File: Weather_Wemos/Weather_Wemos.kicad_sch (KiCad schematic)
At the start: 20 parts, among them J1 Pwr In, J2 12V, J3 Rain 3 Adv, J4 WIND, J5 RAIN 1, J6 Rain 2 Serial, U1 WeMos_D1_mini, U2 L7805

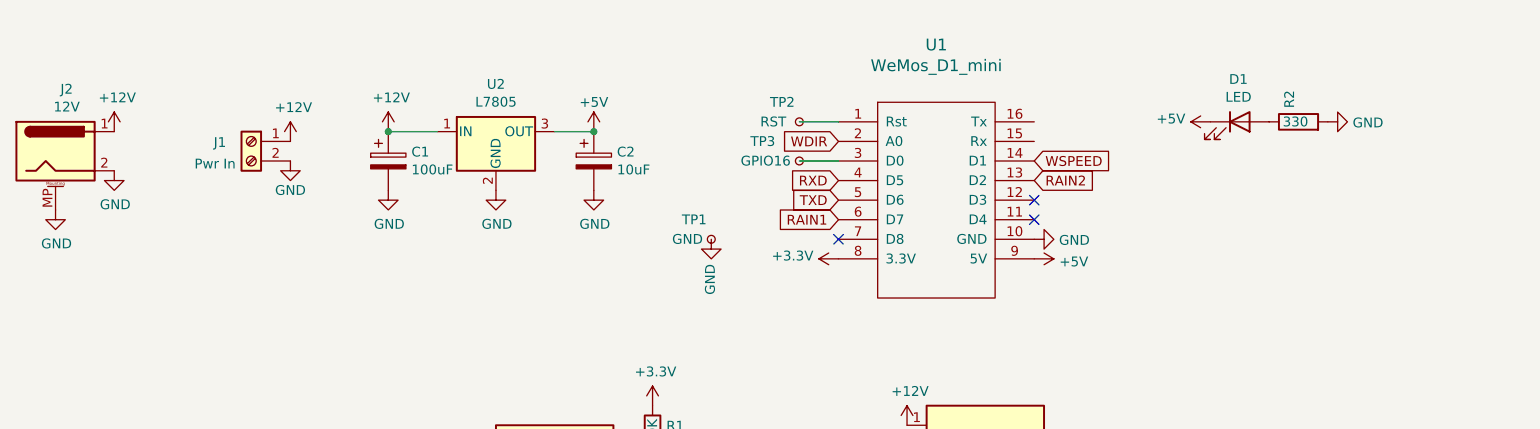
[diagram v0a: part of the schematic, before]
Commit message: added temperature sensor
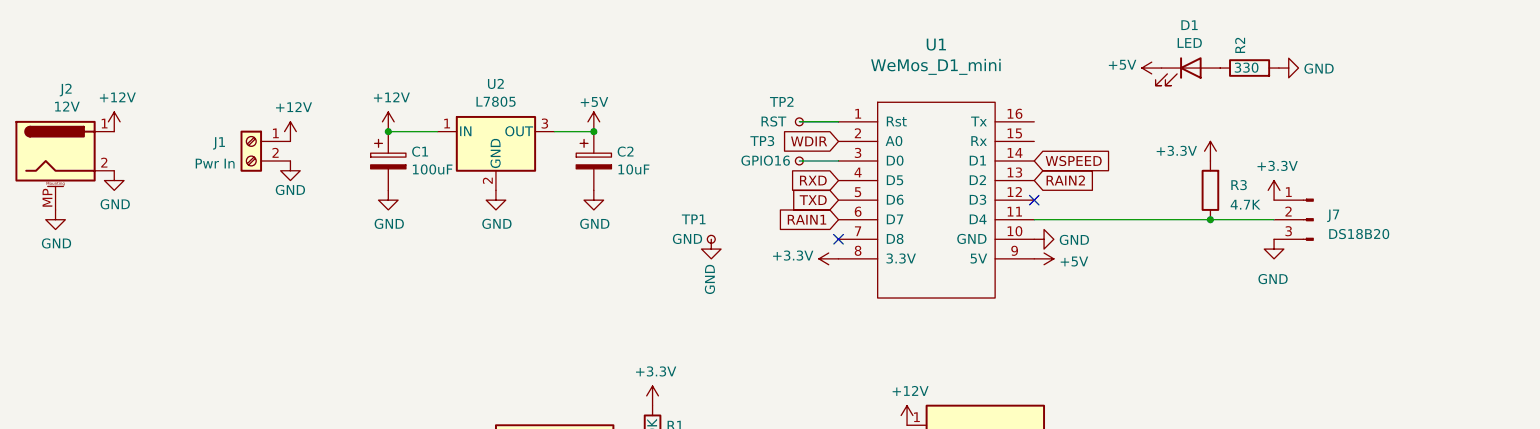
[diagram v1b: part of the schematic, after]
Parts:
- added J7: DS18B20, Connector_JST:JST_XH_B3B-XH-A_1x03_P2.50mm_Vertical, symbol Connector:Conn_01x03_Pin
- added R3: 4.7K, Resistor_THT:R_Axial_DIN0207_L6.3mm_D2.5mm_P7.62mm_Horizontal, symbol Device:R
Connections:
- net +3V3: now also J7.1 (Pin_1), R3.2
- net GND: now also J7.3 (Pin_3)
- net at U1.11 (D4): now also J7.2 (Pin_2), R3.1
- no-connect marks 3 -> 2
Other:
- moved on the sheet: D1, R2

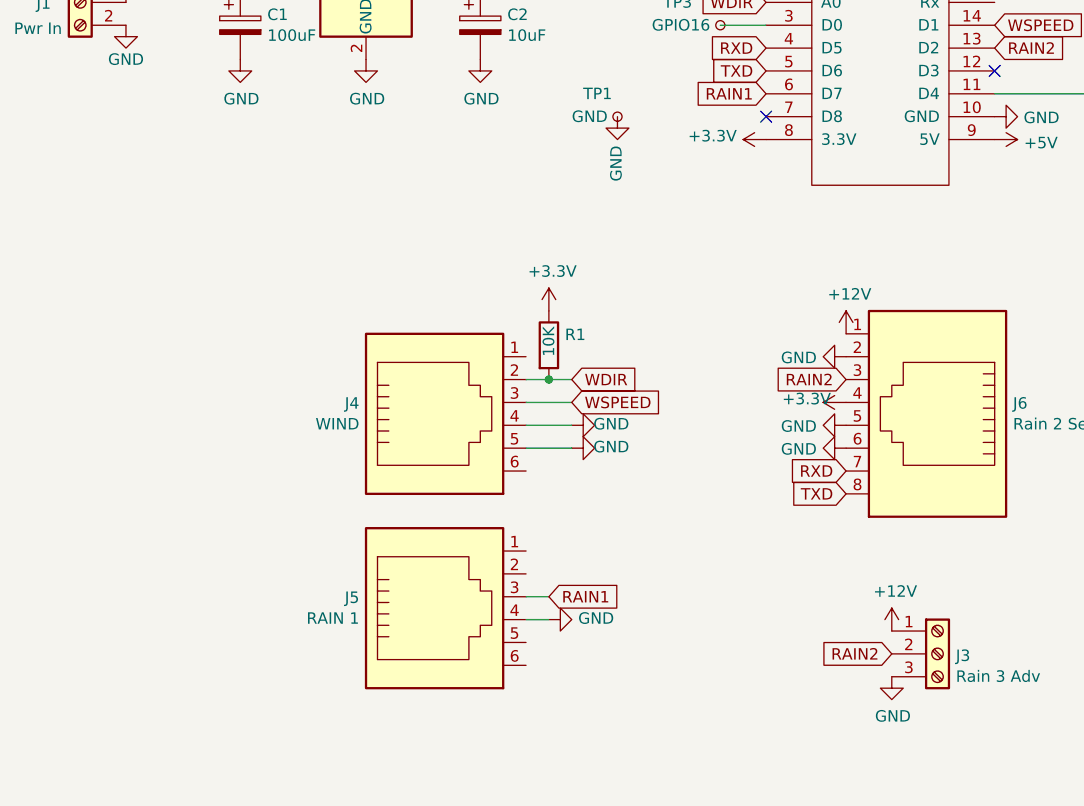
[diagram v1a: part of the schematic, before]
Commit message: add plug in 3 to 4 adapter
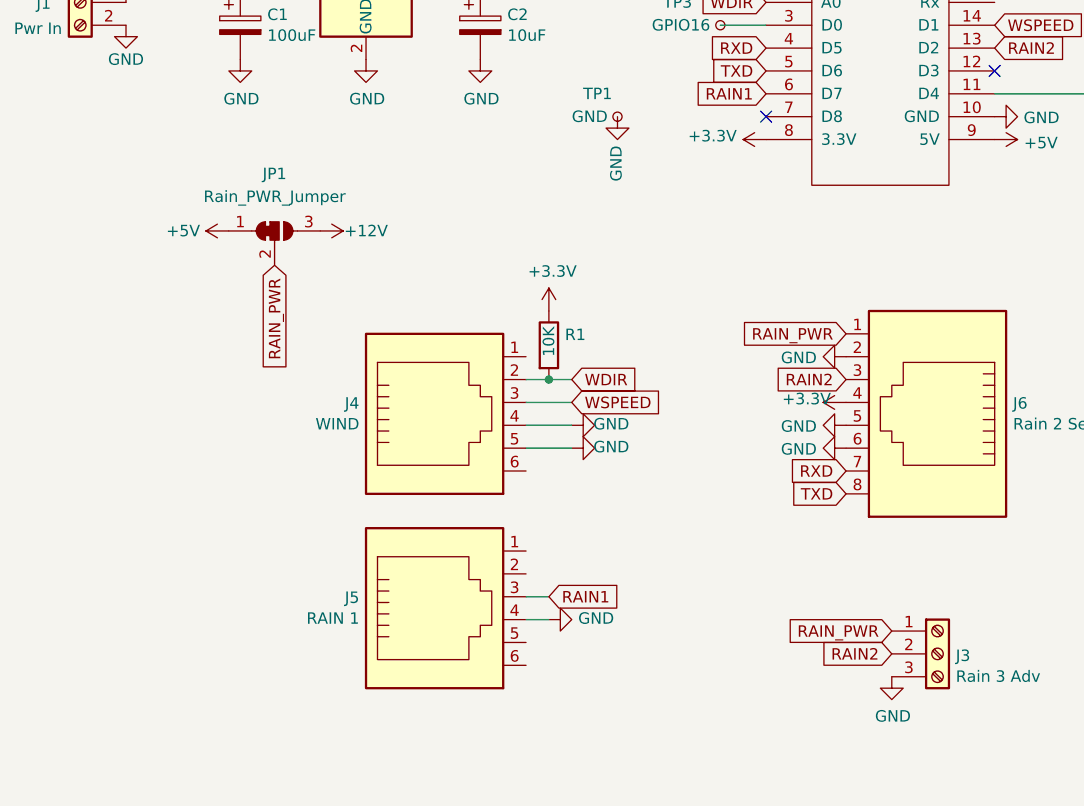
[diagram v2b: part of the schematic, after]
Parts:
- added JP1: Rain_PWR_Jumper, Jumper:SolderJumper-3_P1.3mm_Bridged2Bar12_RoundedPad1.0x1.5mm_NumberLabels, symbol Jumper:SolderJumper_3_Bridged12
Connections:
- net +12V: now also JP1.3 (B); no longer J3.1 (Pin_1), J6.1
- net +5V: now also JP1.1 (A)
- new net RAIN_PWR: J3.1 (Pin_1), J6.1, JP1.2 (C)
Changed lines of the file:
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@@
     (stroke (width 0) (type default))
+  )
+  (global_label "RAIN_PWR" (shape input) (at 144.78 86.36 180) (fields_autoplaced)
+    (effects (font (size 1.27 1.27)) (justify right))
+    (property "Intersheetrefs" "${INTERSHEET_REFS}" (at 133.2755 86.36 0)
+      (effects (font (size 1.27 1.27)) (justify right) hide)
+    )
   )
   (global_label "TXD" (shape input) (at 144.78 104.14 180) (fields_autoplaced)
@@
     )
   )
+  (global_label "RAIN_PWR" (shape input) (at 149.86 119.38 180) (fields_autoplaced)
+    (effects (font (size 1.27 1.27)) (justify right))
+    (property "Intersheetrefs" "${INTERSHEET_REFS}" (at 138.3555 119.38 0)
+      (effects (font (size 1.27 1.27)) (justify right) hide)
+    )
+  )
   (global_label "RAIN2" (shape input) (at 161.29 54.61 0) (fields_autoplaced)
     (effects (font (size 1.27 1.27)) (justify left))
@@
     (property "Intersheetrefs" "${INTERSHEET_REFS}" (at 13.97 59.69 0)
       (effects (font (size 1.27 1.27)) hide)
+    )
+  )
+  (global_label "RAIN_PWR" (shape input) (at 81.28 78.74 270) (fields_autoplaced)
+    (effects (font (size 1.27 1.27)) (justify right))
+    (property "Intersheetrefs" "${INTERSHEET_REFS}" (at 81.28 90.2445 90)
+      (effects (font (size 1.27 1.27)) (justify right) hide)
     )
   )
@@
     )
   )
-  (symbol (lib_id "power:+12V") (at 149.86 119.38 0) (unit 1)
-    (in_bom yes) (on_board yes) (dnp no)
-    (property "Reference" "#PWR018" (at 149.86 123.19 0)
-      (effects (font (size 1.27 1.27)) hide)
-    )
-    (property "Value" "+12V" (at 150.241 114.9858 0)
-      (effects (font (size 1.27 1.27)))
-    )
-    (property "Footprint" "" (at 149.86 119.38 0)
-      (effects (font (size 1.27 1.27)) hide)
-    )
-    (property "Datasheet" "" (at 149.86 119.38 0)
-      (effects (font (size 1.27 1.27)) hide)
-    )
-    (pin "1")
-    (instances
-      (project "Weather_Wemos"
-        (path "/27b2eb82-662b-42d8-90e6-830fec4bb8d2"
-          (reference "#PWR018") (unit 1)
-        )
-      )
-    )
-  )
-  (symbol (lib_id "power:+12V") (at 144.78 86.36 0) (unit 1)
-    (in_bom yes) (on_board yes) (dnp no)
-    (property "Reference" "#PWR013" (at 144.78 90.17 0)
-      (effects (font (size 1.27 1.27)) hide)
-    )
-    (property "Value" "+12V" (at 145.161 81.9658 0)
-      (effects (font (size 1.27 1.27)))
-    )
-    (property "Footprint" "" (at 144.78 86.36 0)
-      (effects (font (size 1.27 1.27)) hide)
-    )
-    (property "Datasheet" "" (at 144.78 86.36 0)
-      (effects (font (size 1.27 1.27)) hide)
-    )
-    (pin "1")
-    (instances
-      (project "Weather_Wemos"
-        (path "/27b2eb82-662b-42d8-90e6-830fec4bb8d2"
-          (reference "#PWR013") (unit 1)
-        )
-      )
-    )
-  )
   (symbol (lib_id "power:GND") (at 144.78 88.9 270) (unit 1)
     (in_bom yes) (on_board yes) (dnp no)
@@
     )
   )
+  (symbol (lib_id "power:+12V") (at 86.36 74.93 270) (unit 1)
+    (in_bom yes) (on_board yes) (dnp no)
+    (property "Reference" "#PWR023" (at 82.55 74.93 0)
+      (effects (font (size 1.27 1.27)) hide)
+    )
+    (property "Value" "+12V" (at 91.44 74.93 90)
+      (effects (font (size 1.27 1.27)))
+    )
+    (property "Footprint" "" (at 86.36 74.93 0)
+      (effects (font (size 1.27 1.27)) hide)
+    )
+    (property "Datasheet" "" (at 86.36 74.93 0)
+      (effects (font (size 1.27 1.27)) hide)
+    )
+    (pin "1")
+    (instances
+      (project "Weather_Wemos"
+        (path "/27b2eb82-662b-42d8-90e6-830fec4bb8d2"
+          (reference "#PWR023") (unit 1)
+        )
+      )
+    )
+  )
   (symbol (lib_id "Device:R") (at 184.15 55.88 180) (unit 1)
     (in_bom yes) (on_board yes) (dnp no) (fields_autoplaced)
@@
     )
   )
+  (symbol (lib_id "power:+5V") (at 76.2 74.93 90) (unit 1)
+    (in_bom yes) (on_board yes) (dnp no)
+    (property "Reference" "#PWR022" (at 80.01 74.93 0)
+      (effects (font (size 1.27 1.27)) hide)
+    )
+    (property "Value" "+5V" (at 71.12 74.93 90)
+      (effects (font (size 1.27 1.27)))
+    )
+    (property "Footprint" "" (at 76.2 74.93 0)
+      (effects (font (size 1.27 1.27)) hide)
+    )
+    (property "Datasheet" "" (at 76.2 74.93 0)
+      (effects (font (size 1.27 1.27)) hide)
+    )
+    (pin "1")
+    (instances
+      (project "Weather_Wemos"
+        (path "/27b2eb82-662b-42d8-90e6-830fec4bb8d2"
+          (reference "#PWR022") (unit 1)
+        )
+      )
+    )
+  )
   (symbol (lib_id "power:+3.3V") (at 192.405 57.15 0) (unit 1)
     (in_bom yes) (on_board yes) (dnp no)
@@
         )
       )
+    )
+  )
+  (symbol (lib_id "Jumper:SolderJumper_3_Bridged12") (at 81.28 74.93 0) (unit 1)
+    (in_bom no) (on_board yes) (dnp no) (fields_autoplaced)
+    (property "Reference" "JP1" (at 81.28 68.58 0)
+      (effects (font (size 1.27 1.27)))
+    )
+    (property "Value" "Rain_PWR_Jumper" (at 81.28 71.12 0)
+      (effects (font (size 1.27 1.27)))
+    )
+    (property "Footprint" "Jumper:SolderJumper-3_P1.3mm_Bridged2Bar12_RoundedPad1.0x1.5mm_NumberLabels" (at 81.28 74.93 0)
+      (effects (font (size 1.27 1.27)) hide)
+    )
+    (property "Datasheet" "~" (at 81.28 74.93 0)
+      (effects (font (size 1.27 1.27)) hide)
+    )
+    (property "LCSC" "" (at 81.28 74.93 0)
+      (effects (font (size 1.27 1.27)))
+    )
+    (pin "1")
+    (pin "2")
+    (pin "3")
+    (instances
+      (project "Weather_Wemos"
+        (path "/27b2eb82-662b-42d8-90e6-830fec4bb8d2"
+          (reference "JP1") (unit 1)
+        )
+      )
